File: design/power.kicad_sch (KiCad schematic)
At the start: 37 parts, among them J10 PJ-002BH, U4 TPS7A2050PDQN, U5 TPS7A2033PDQN, U6 LMR33630ADDA, U7 LMR33630ADDA

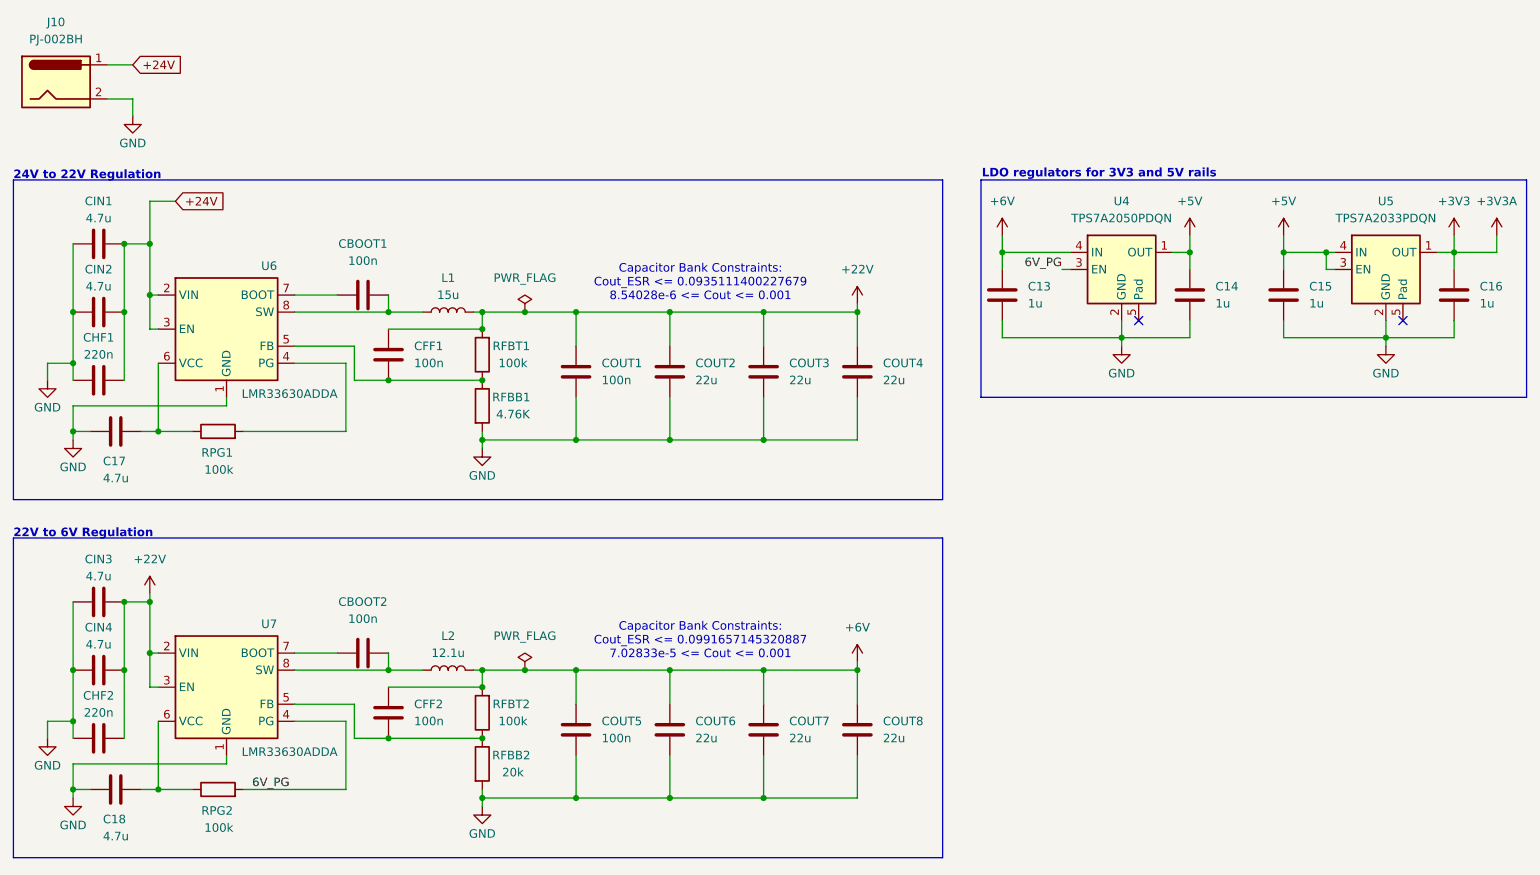
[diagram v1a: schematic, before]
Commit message: added ferrite bead between HVGND and GND
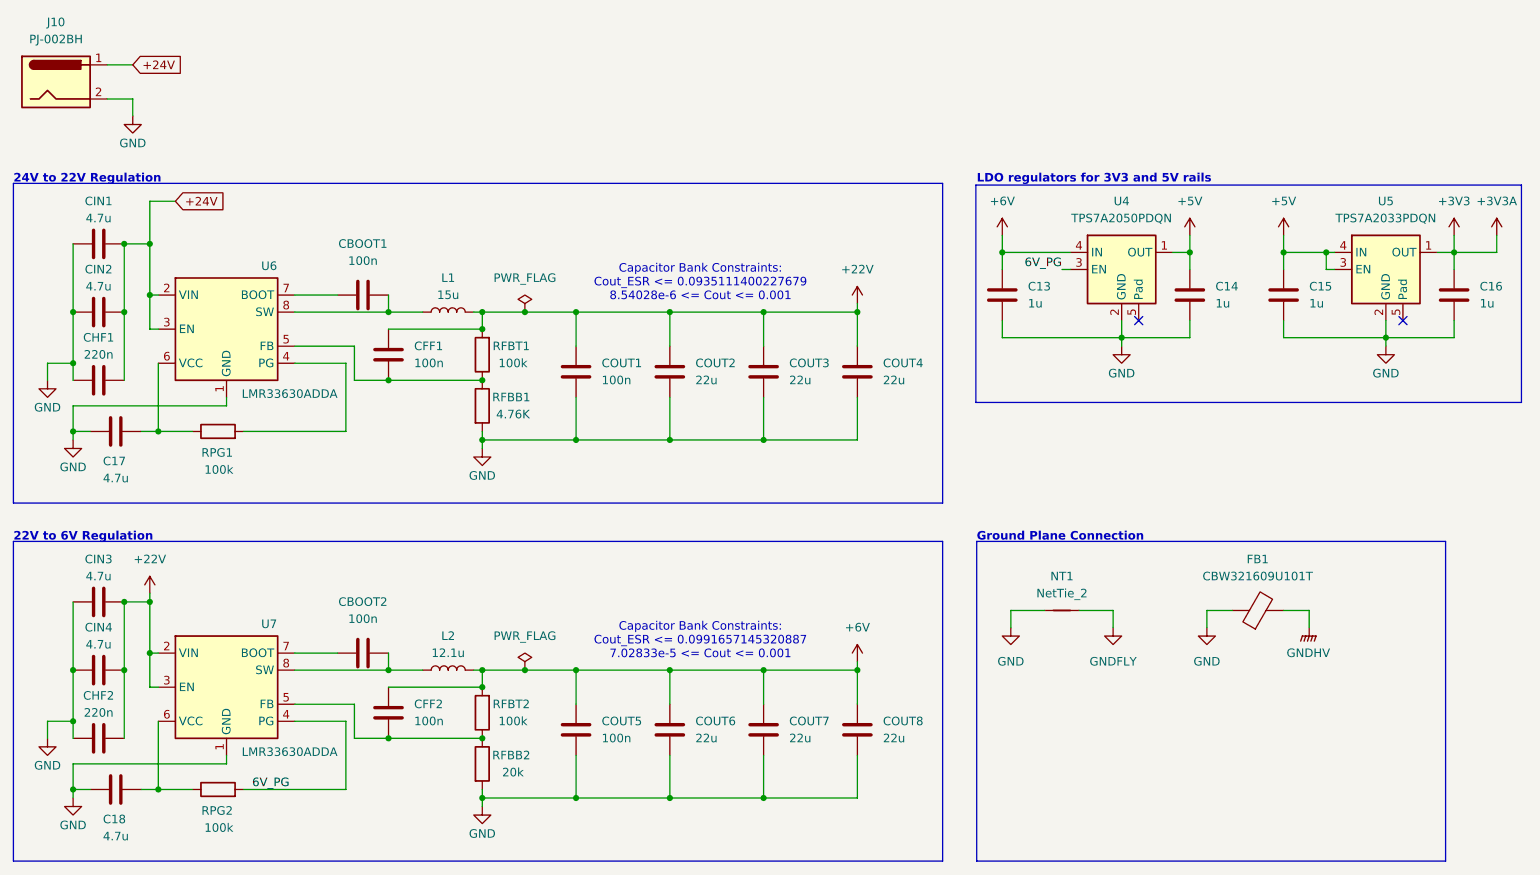
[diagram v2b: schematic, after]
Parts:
- added FB1: CBW321609U101T, Inductor_SMD:L_1206_3216Metric, symbol Device:FerriteBead
- added NT1: NetTie_2, NetTie:NetTie-2_SMD_Pad2.0mm, symbol Device:NetTie_2
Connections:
- net GND: now also FB1.1, NT1.1
- new net GNDFLY: NT1.2
- new net GNDHV: FB1.2
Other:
- note added: "Ground Plane Connection"

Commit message: _
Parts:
- C14, C16: value 1u -> 5u
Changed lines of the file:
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@@
 	(text "Capacitor Bank Constraints:\nCout_ESR <= 0.0991657145320887\n7.02833e-5 <= Cout <= 0.001"
 		(exclude_from_sim no)
-		(at 117.602 107.442 0)
+		(at 117.602 102.362 0)
 		(effects
 			(font
@@
 	(text "Capacitor Bank Constraints:\nCout_ESR <= 0.0935111400227679\n8.54028e-6 <= Cout <= 0.001"
 		(exclude_from_sim no)
-		(at 117.602 54.102 0)
+		(at 117.602 49.022 0)
 		(effects
 			(font
@@
 			)
 		)
-		(property "Value" "1u"
+		(property "Value" "5u"
 			(at 194.31 57.1499 0)
 			(show_name no)
@@
 			)
 		)
-		(property "Value" "1u"
+		(property "Value" "5u"
 			(at 233.68 57.1499 0)
 			(show_name no)

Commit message: Rev 0.2 Production
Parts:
- C14, C16: value 5u -> 1u
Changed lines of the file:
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@@
 			)
 		)
-		(property "Value" "5u"
+		(property "Value" "1u"
 			(at 194.31 57.1499 0)
 			(show_name no)
@@
 			)
 		)
-		(property "Value" "5u"
+		(property "Value" "1u"
 			(at 233.68 57.1499 0)
 			(show_name no)
